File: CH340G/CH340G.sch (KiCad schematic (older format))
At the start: 24 parts, among them J2 Conn_01x06, P1 USB_C_Plug_USB2.0, U1 CH340G, U2 AP2127K-3.3, Y1 Crystal_GND24

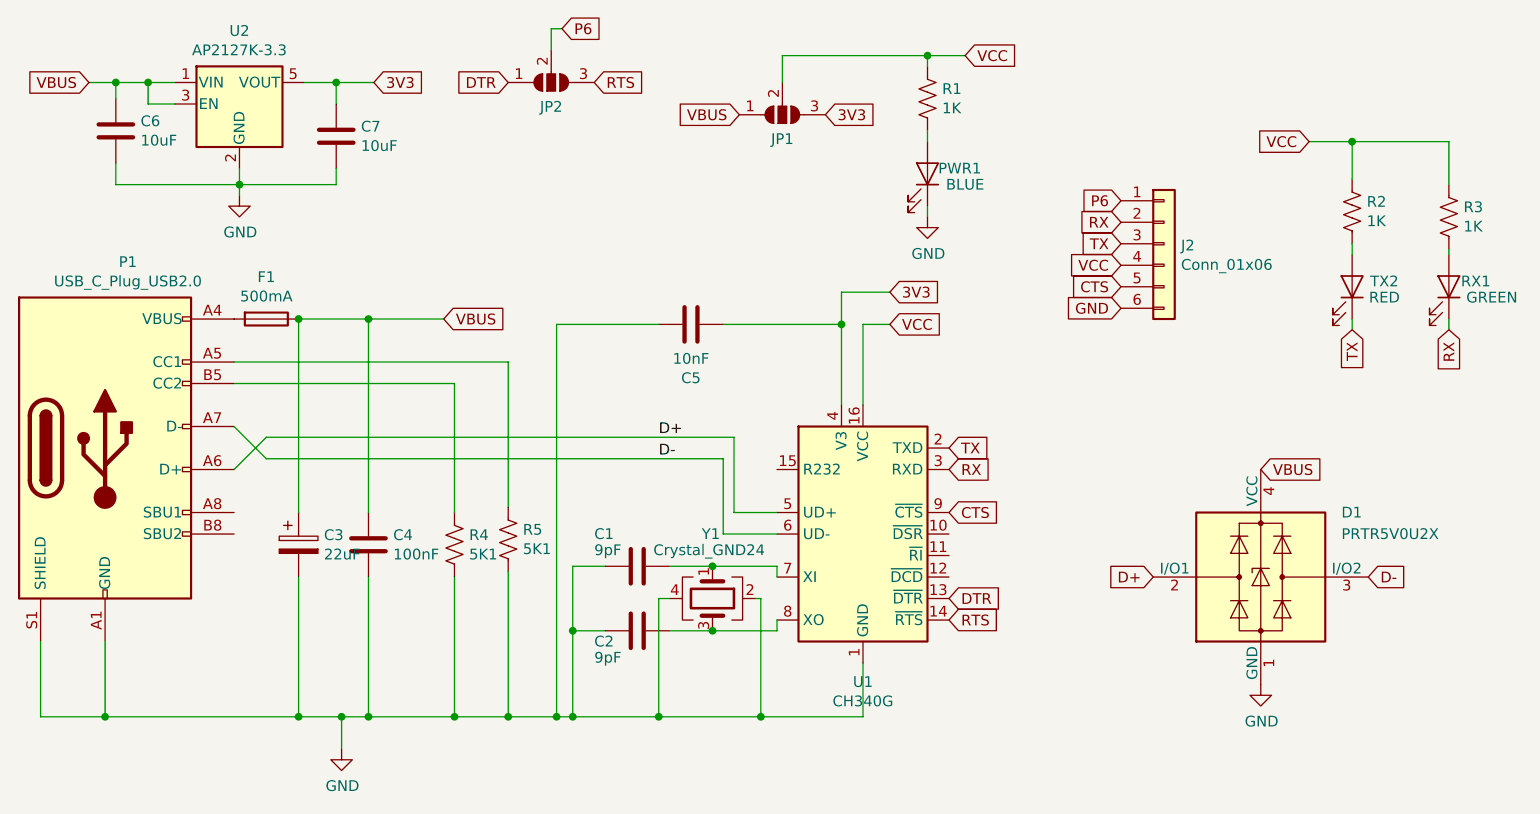
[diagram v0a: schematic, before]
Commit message: SirUSB Board Revisions
Removed MicroUSB Versions of FT230 and FT231, SolderPaste Layer Adjusted to -0.05mm, Silkscreens optimised, OSHW logo added.
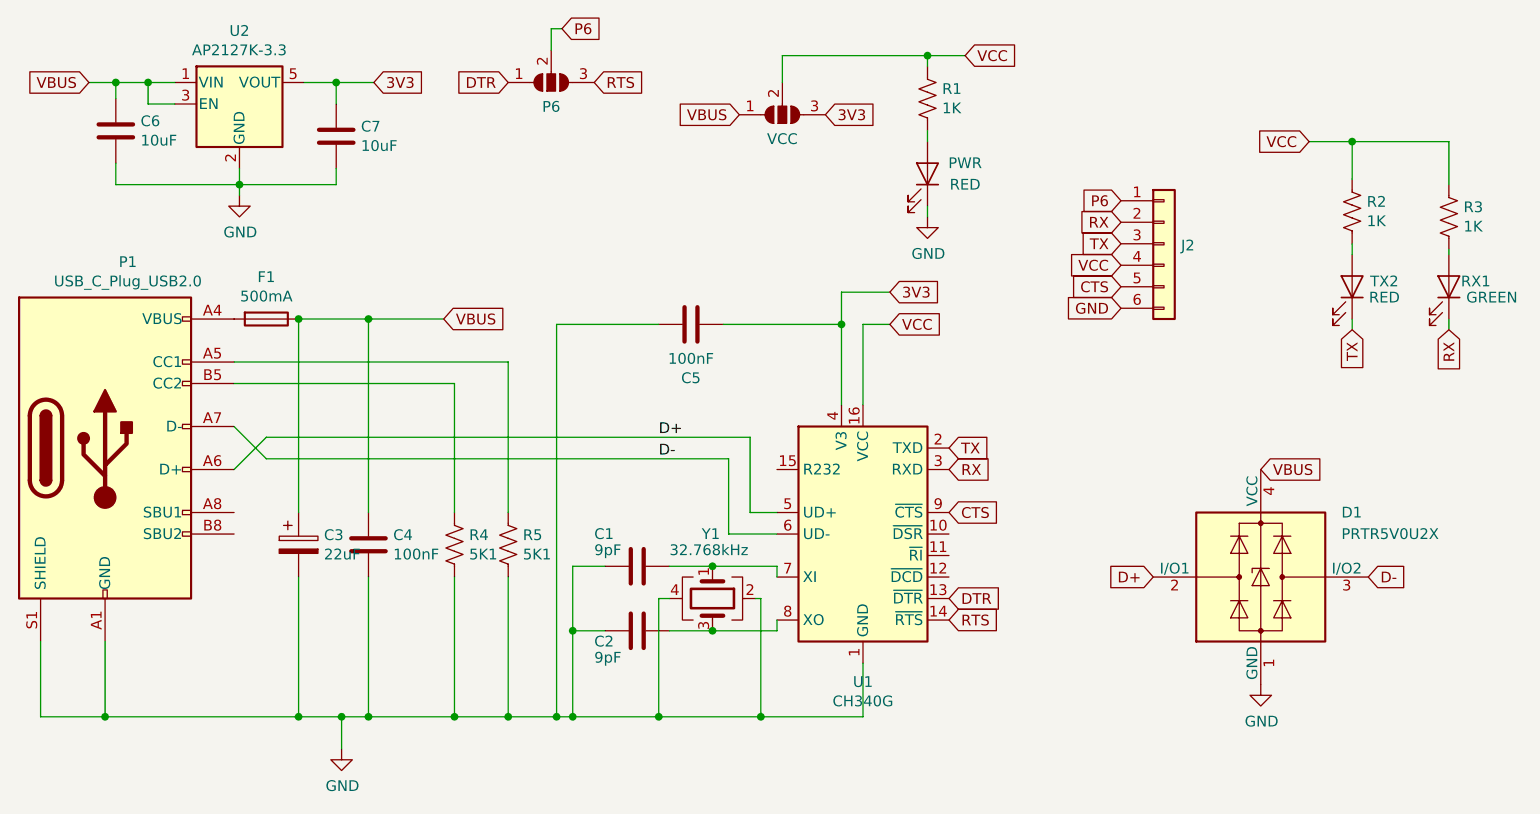
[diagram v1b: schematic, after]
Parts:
- C5: value 10nF -> 100nF; Part C100042 -> C42998
- PWR: renamed from PWR1; value BLUE -> RED; Part C193191 -> C118330
- Y1: value Crystal_GND24 -> 32.768kHz
- renumbered JP2 to P6, JP1 to VCC
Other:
- moved on the sheet: R5
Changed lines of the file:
@@
 P 6025 1700
 F 0 "J2" H 6104 1692 50  0000 L CNN
-F 1 "Conn_01x06" H 6104 1602 50  0000 L CNN
+F 1 "Conn_01x06" H 6104 1602 50  0001 L CNN
 F 2 "Connector_PinHeader_2.54mm:PinHeader_1x06_P2.54mm_Horizontal" H 6025 1700 50  0001 C CNN
 F 3 "~" H 6025 1700 50  0001 C CNN
@@
 $EndComp
 $Comp
-L Jumper:SolderJumper_3_Open JP2
+L Jumper:SolderJumper_3_Open P6
 U 1 1 5D651B6F
 P 3175 950
-F 0 "JP2" H 3175 1063 50  0000 C CNN
+F 0 "P6" H 3175 1063 50  0000 C CNN
 F 1 "SolderJumper_3_Open" H 3175 1063 50  0001 C CNN
 F 2 "Jumper:SolderJumper-3_P1.3mm_Open_RoundedPad1.0x1.5mm" H 3175 950 50  0001 C CNN
@@
 	4625 3650 4625 3900
 Wire Wire Line
-	4225 2950 4025 2950
-Wire Wire Line
-	4025 2950 4025 2600
-Wire Wire Line
-	3975 2700 3975 3050
-Wire Wire Line
-	3975 3050 4225 3050
+	4225 2950 4100 2950
+Wire Wire Line
+	4100 2950 4100 2600
+Wire Wire Line
+	4000 2700 4000 3050
+Wire Wire Line
+	4000 3050 4225 3050
 Wire Wire Line
 	2000 2950 2000 2050
@@
 	1850 2600 1700 2750
 Wire Wire Line
-	1850 2600 4025 2600
+	1850 2600 4100 2600
 Wire Wire Line
 	1850 2700 1700 2550
 Wire Wire Line
-	1850 2700 3975 2700
+	1850 2700 4000 2700
 Wire Wire Line
 	800  3550 800  3900
@@
 P 3825 2075
 F 0 "C5" V 4075 2075 50  0000 C CNN
-F 1 "10nF" V 3985 2075 50  0000 C CNN
+F 1 "100nF" V 3985 2075 50  0000 C CNN
 F 2 "Capacitor_SMD:C_0603_1608Metric" H 3863 1925 50  0001 C CNN
 F 3 "~" H 3825 2075 50  0001 C CNN
-F 4 "C100042" V 3825 2075 50  0001 C CNN "Part"
+F 4 "C42998" V 3825 2075 50  0001 C CNN "Part"
 	1    3825 2075
 	0    -1   1    0
@@
 P 3925 3350
 F 0 "Y1" V 3625 3300 50  0000 L CNN
-F 1 "Crystal_GND24" V 3700 3075 50  0000 L CNN
+F 1 "32.768kHz" V 3700 3150 50  0000 L CNN
 F 2 "Crystal:Crystal_SMD_SeikoEpson_TSX3225-4Pin_3.2x2.5mm" H 3925 3350 50  0001 C CNN
 F 3 "~" H 3925 3350 50  0001 C CNN
@@
 $EndComp
 $Comp
-L Jumper:SolderJumper_3_Open JP1
+L Jumper:SolderJumper_3_Open VCC
 U 1 1 5D65075B
 P 4250 1100
-F 0 "JP1" H 4250 1213 50  0000 C CNN
+F 0 "VCC" H 4250 1213 50  0000 C CNN
 F 1 "SolderJumper_3_Open" H 4250 1213 50  0001 C CNN
 F 2 "Jumper:SolderJumper-3_P1.3mm_Open_RoundedPad1.0x1.5mm" H 4250 1100 50  0001 C CNN
@@
 $EndComp
 $Comp
-L Device:LED PWR1
+L Device:LED PWR
 U 1 1 5E4F8641
 P 4925 1375
-F 0 "PWR1" V 4950 1525 50  0000 C CNN
-F 1 "BLUE" V 4875 1550 50  0000 C CNN
+F 0 "PWR" V 4975 1550 50  0000 C CNN
+F 1 "RED" V 4875 1550 50  0000 C CNN
 F 2 "LED_SMD:LED_0603_1608Metric" H 4925 1375 50  0001 C CNN
 F 3 "~" H 4925 1375 50  0001 C CNN
-F 4 "C193191" H 4925 1375 50  0001 C CNN "Part"
+F 4 "C118330" H 4925 1375 50  0001 C CNN "Part"
 	1    4925 1375
 	0    1    -1   0
@@
 L Device:R_US R5
 U 1 1 5E8EA1B4
-P 2975 3075
-F 0 "R5" H 3043 3120 50  0000 L CNN
-F 1 "5K1" H 3043 3030 50  0000 L CNN
-F 2 "Resistor_SMD:R_0603_1608Metric" V 3015 3065 50  0001 C CNN
-F 3 "~" H 2975 3075 50  0001 C CNN
-F 4 "C332117" H 2975 3075 50  0001 C CNN "Part"
-	1    2975 3075
+P 2975 3100
+F 0 "R5" H 3043 3145 50  0000 L CNN
+F 1 "5K1" H 3043 3055 50  0000 L CNN
+F 2 "Resistor_SMD:R_0603_1608Metric" V 3015 3090 50  0001 C CNN
+F 3 "~" H 2975 3100 50  0001 C CNN
+F 4 "C332117" H 2975 3100 50  0001 C CNN "Part"
+	1    2975 3100
 	1    0    0    -1
 $EndComp
@@
 	1700 2250 2975 2250
 Wire Wire Line
-	2975 2250 2975 2925
+	2975 2250 2975 2950
 Wire Wire Line
 	2725 3250 2725 3900
@@
 	2725 3900 2975 3900
 Wire Wire Line
-	2975 3225 2975 3900
+	2975 3250 2975 3900
 Connection ~ 2975 3900
 Wire Wire Line
